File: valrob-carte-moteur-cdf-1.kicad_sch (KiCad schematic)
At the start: 48 parts, among them J1 USB_C_Receptacle_USB2.0_14P, J2 Conn_01x02, J3 Conn_01x02, J4 Conn_01x04_Pin, J5 Conn_01x08, J6 Conn_01x02, J7 Conn_01x02, J8 Conn_01x08, SW1 SW_Push, SW2 SW_Push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

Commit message: schem: add components footprints
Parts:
- C4, C7: footprint (none) -> Capacitor_SMD:C_0603_1608Metric
- C6: footprint (none) -> Capacitor_SMD:C_0805_2012Metric
- D4: footprint (none) -> Diode_SMD:D_SOD-123
- J2, J3, J6, J7: footprint (none) -> Connector_JST:JST_XH_S2B-XH-A_1x02_P2.50mm_Horizontal
- J5, J8: footprint (none) -> Connector_Molex:Molex_PicoBlade_53048-0810_1x08_P1.25mm_Horizontal
- R4: footprint (none) -> Resistor_SMD:R_0603_1608Metric
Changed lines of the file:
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@@
 			)
 		)
-		(property "Footprint" ""
+		(property "Footprint" "Connector_JST:JST_XH_S2B-XH-A_1x02_P2.50mm_Horizontal"
 			(at 87.63 180.34 0)
 			(effects
@@
 			)
 		)
-		(property "Footprint" ""
+		(property "Footprint" "Connector_Molex:Molex_PicoBlade_53048-0810_1x08_P1.25mm_Horizontal"
 			(at 50.8 95.25 0)
 			(effects
@@
 			)
 		)
-		(property "Footprint" ""
+		(property "Footprint" "Diode_SMD:D_SOD-123"
 			(at 109.22 148.59 0)
 			(effects
@@
 			)
 		)
-		(property "Footprint" ""
+		(property "Footprint" "Connector_JST:JST_XH_S2B-XH-A_1x02_P2.50mm_Horizontal"
 			(at 266.7 114.3 0)
 			(effects
@@
 			)
 		)
-		(property "Footprint" ""
+		(property "Footprint" "Connector_Molex:Molex_PicoBlade_53048-0810_1x08_P1.25mm_Horizontal"
 			(at 90.17 95.25 0)
 			(effects
@@
 			)
 		)
-		(property "Footprint" ""
+		(property "Footprint" "Capacitor_SMD:C_0603_1608Metric"
 			(at 180.0352 40.64 0)
 			(effects
@@
 			)
 		)
-		(property "Footprint" ""
+		(property "Footprint" "Resistor_SMD:R_0603_1608Metric"
 			(at 98.552 148.59 90)
 			(effects
@@
 			)
 		)
-		(property "Footprint" ""
+		(property "Footprint" "Connector_JST:JST_XH_S2B-XH-A_1x02_P2.50mm_Horizontal"
 			(at 266.7 83.82 0)
 			(effects
@@
 			)
 		)
-		(property "Footprint" ""
+		(property "Footprint" "Capacitor_SMD:C_0603_1608Metric"
 			(at 90.4748 152.4 0)
 			(effects
@@
 			)
 		)
-		(property "Footprint" ""
+		(property "Footprint" "Connector_JST:JST_XH_S2B-XH-A_1x02_P2.50mm_Horizontal"
 			(at 107.95 180.34 0)
 			(effects
@@
 			)
 		)
-		(property "Footprint" ""
+		(property "Footprint" "Capacitor_SMD:C_0805_2012Metric"
 			(at 170.4848 40.64 0)
 			(effects

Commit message: schem: add ordering info to BOM
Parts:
- C3: footprint Capacitor_SMD:C_0402_1005Metric -> Capacitor_SMD:C_0603_1608Metric; JLCPCB Part # C15525 -> C19702; Manufacturer Part Number CL05A106MQ5NUNC -> CL10A106KP8NNNC
- C4, C7: Basic (none) -> Y; JLCPCB Part # (none) -> C14663; Manufacturer (none) -> YAGEO; Manufacturer Part Number (none) -> CC0603KRX7R9BB104
- C5: footprint Capacitor_SMD:C_0402_1005Metric -> Capacitor_SMD:C_0603_1608Metric; JLCPCB Part # C52923 -> C15849; Manufacturer Part Number CL05A105KA5NQNC -> CL10A105KB8NNNC
- C6: Basic (none) -> Y; JLCPCB Part # (none) -> C45783; Manufacturer (none) -> Samsung Electro-Mechanics; Manufacturer Part Number (none) -> CL21A226MAQNNNE
- D4: Basic (none) -> E; JLCPCB Part # (none) -> C19077392; Manufacturer (none) -> hongjiacheng; Manufacturer Part Number (none) -> BZT52B3V3
- J2, J3, J5, J6, J7, J8, U3: now left out of the parts list
- R4: Basic (none) -> Y; JLCPCB Part # (none) -> C22978; Manufacturer (none) -> Uniroyal Elec; Manufacturer Part Number (none) -> 0603WAF3301T5E
- R8, R9: footprint Resistor_SMD:R_0402_1005Metric -> Resistor_SMD:R_0603_1608Metric; JLCPCB Part # C25092 -> C23345; Manufacturer Part Number 0402WGF220JTCE -> 0603WAF220JT5E
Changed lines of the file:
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@@
 			)
 		)
-		(property "Footprint" "Capacitor_SMD:C_0402_1005Metric"
+		(property "Footprint" "Capacitor_SMD:C_0603_1608Metric"
 			(at 61.2648 135.89 0)
 			(effects
@@
 			)
 		)
-		(property "Manufacturer Part Number" "CL05A106MQ5NUNC"
+		(property "Manufacturer Part Number" "CL10A106KP8NNNC"
 			(at 62.23 132.08 0)
 			(effects
@@
 			)
 		)
-		(property "JLCPCB Part #" "C15525"
+		(property "JLCPCB Part #" "C19702"
 			(at 62.23 132.08 0)
 			(effects
@@
 		(unit 1)
 		(exclude_from_sim no)
-		(in_bom yes)
+		(in_bom no)
 		(on_board yes)
 		(dnp no)
@@
 			)
 		)
-		(property "Footprint" "Resistor_SMD:R_0402_1005Metric"
+		(property "Footprint" "Resistor_SMD:R_0603_1608Metric"
 			(at 247.65 61.722 90)
 			(effects
@@
 			)
 		)
-		(property "JLCPCB Part #" "C25092"
+		(property "JLCPCB Part #" "C23345"
 			(at 247.65 63.5 90)
 			(effects
@@
 			)
 		)
-		(property "Manufacturer Part Number" "0402WGF220JTCE"
+		(property "Manufacturer Part Number" "0603WAF220JT5E"
 			(at 247.65 63.5 90)
 			(effects
@@
 		(unit 1)
 		(exclude_from_sim no)
-		(in_bom yes)
+		(in_bom no)
 		(on_board yes)
 		(dnp no)
@@
 			)
 		)
-		(property "Footprint" "Resistor_SMD:R_0402_1005Metric"
+		(property "Footprint" "Resistor_SMD:R_0603_1608Metric"
 			(at 247.65 62.738 90)
 			(effects
@@
 			)
 		)
-		(property "JLCPCB Part #" "C25092"
+		(property "JLCPCB Part #" "C23345"
 			(at 247.65 60.96 90)
 			(effects
@@
 			)
 		)
-		(property "Manufacturer Part Number" "0402WGF220JTCE"
+		(property "Manufacturer Part Number" "0603WAF220JT5E"
 			(at 247.65 60.96 90)
 			(effects
@@
 			)
 		)
+		(property "Basic" "E"
+			(at 109.22 148.59 90)
+			(effects
+				(font
+					(size 1.27 1.27)
+				)
+				(hide yes)
+			)
+		)
+		(property "JLCPCB Part #" "C19077392"
+			(at 109.22 148.59 90)
+			(effects
+				(font
+					(size 1.27 1.27)
+				)
+				(hide yes)
+			)
+		)
+		(property "Manufacturer" "hongjiacheng"
+			(at 109.22 148.59 90)
+			(effects
+				(font
+					(size 1.27 1.27)
+				)
+				(hide yes)
+			)
+		)
+		(property "Manufacturer Part Number" "BZT52B3V3"
+			(at 109.22 148.59 90)
+			(effects
+				(font
+					(size 1.27 1.27)
+				)
+				(hide yes)
+			)
+		)
 		(pin "1"
 		)
@@
 		(unit 1)
 		(exclude_from_sim no)
-		(in_bom yes)
+		(in_bom no)
 		(on_board yes)
 		(dnp no)
@@
 		(unit 1)
 		(exclude_from_sim no)
-		(in_bom yes)
+		(in_bom no)
 		(on_board yes)
 		(dnp no)
@@
 		(unit 1)
 		(exclude_from_sim no)
-		(in_bom yes)
+		(in_bom no)
 		(on_board yes)
 		(dnp no)
@@
 			)
 		)
+		(property "Basic" "Y"
+			(at 179.07 36.83 0)
+			(effects
+				(font
+					(size 1.27 1.27)
+				)
+				(hide yes)
+			)
+		)
+		(property "JLCPCB Part #" "C14663"
+			(at 179.07 36.83 0)
+			(effects
+				(font
+					(size 1.27 1.27)
+				)
+				(hide yes)
+			)
+		)
+		(property "Manufacturer" "YAGEO"
+			(at 179.07 36.83 0)
+			(effects
+				(font
+					(size 1.27 1.27)
+				)
+				(hide yes)
+			)
+		)
+		(property "Manufacturer Part Number" "CC0603KRX7R9BB104"
+			(at 179.07 36.83 0)
+			(effects
+				(font
+					(size 1.27 1.27)
+				)
+				(hide yes)
+			)
+		)
 		(pin "2"
 		)
@@
 			)
 		)
+		(property "Basic" "Y"
+			(at 100.33 148.59 0)
+			(effects
+				(font
+					(size 1.27 1.27)
+				)
+				(hide yes)
+			)
+		)
+		(property "JLCPCB Part #" "C22978"
+			(at 100.33 148.59 0)
+			(effects
+				(font
+					(size 1.27 1.27)
+				)
+				(hide yes)
+			)
+		)
+		(property "Manufacturer" "Uniroyal Elec"
+			(at 100.33 148.59 0)
+			(effects
+				(font
+					(size 1.27 1.27)
+				)
+				(hide yes)
+			)
+		)
+		(property "Manufacturer Part Number" "0603WAF3301T5E"
+			(at 100.33 148.59 0)
+			(effects
+				(font
+					(size 1.27 1.27)
+				)
+				(hide yes)
+			)
+		)
 		(pin "2"
 		)
@@
 		(unit 1)
 		(exclude_from_sim no)
-		(in_bom yes)
+		(in_bom no)
 		(on_board yes)
 		(dnp no)
@@
 			)
 		)
-		(property "Footprint" "Capacitor_SMD:C_0402_1005Metric"
+		(property "Footprint" "Capacitor_SMD:C_0603_1608Metric"
 			(at 129.8448 63.5 0)
 			(effects
@@
 			)
 		)
-		(property "Manufacturer Part Number" "CL05A105KA5NQNC"
+		(property "Manufacturer Part Number" "CL10A105KB8NNNC"
 			(at 130.81 59.69 0)
 			(effects
@@
 			)
 		)
-		(property "JLCPCB Part #" "C52923"
+		(property "JLCPCB Part #" "C15849"
 			(at 130.81 59.69 0)
 			(effects
@@
 			)
 		)
+		(property "Basic" "Y"
+			(at 91.44 148.59 0)
+			(effects
+				(font
+					(size 1.27 1.27)
+				)
+				(hide yes)
+			)
+		)
+		(property "JLCPCB Part #" "C14663"
+			(at 91.44 148.59 0)
+			(effects
+				(font
+					(size 1.27 1.27)
+				)
+				(hide yes)
+			)
+		)
+		(property "Manufacturer" "YAGEO"
+			(at 91.44 148.59 0)
+			(effects
+				(font
+					(size 1.27 1.27)
+				)
+				(hide yes)
+			)
+		)
+		(property "Manufacturer Part Number" "CC0603KRX7R9BB104"
+			(at 91.44 148.59 0)
+			(effects
+				(font
+					(size 1.27 1.27)
+				)
+				(hide yes)
+			)
+		)
 		(pin "2"
 		)
@@
 		(unit 1)
 		(exclude_from_sim no)
-		(in_bom yes)
+		(in_bom no)
 		(on_board yes)
 		(dnp no)
@@
 			(at 171.45 36.83 0)
 			(effects
+				(font
+					(size 1.27 1.27)
+				)
+				(hide yes)
+			)
+		)
+		(property "Basic" "Y"
+			(at 171.45 36.83 0)
+			(effects
+				(font
+					(size 1.27 1.27)
+				)
+				(hide yes)
+			)
+		)
+		(property "JLCPCB Part #" "C45783"
+			(at 171.45 36.83 0)
+			(effects
+				(font
+					(size 1.27 1.27)
+				)
+				(hide yes)
+			)
+		)
+		(property "Manufacturer" "Samsung Electro-Mechanics "
+			(at 171.45 36.83 0)
+			(effects
+				(font
+					(size 1.27 1.27)
+				)
+				(hide yes)
+			)
+		)
+		(property "Manufacturer Part Number" "CL21A226MAQNNNE"
+			(at 171.45 36.83 0)
+			(effects

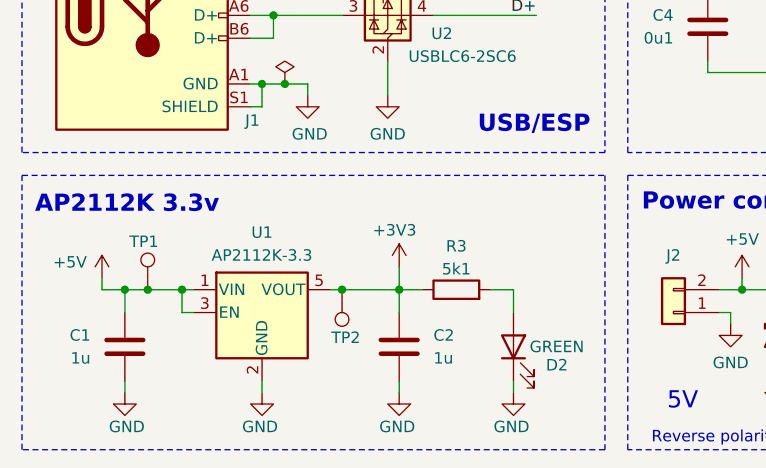
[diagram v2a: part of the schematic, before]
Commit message: schem: add ldo reverse current protection diode
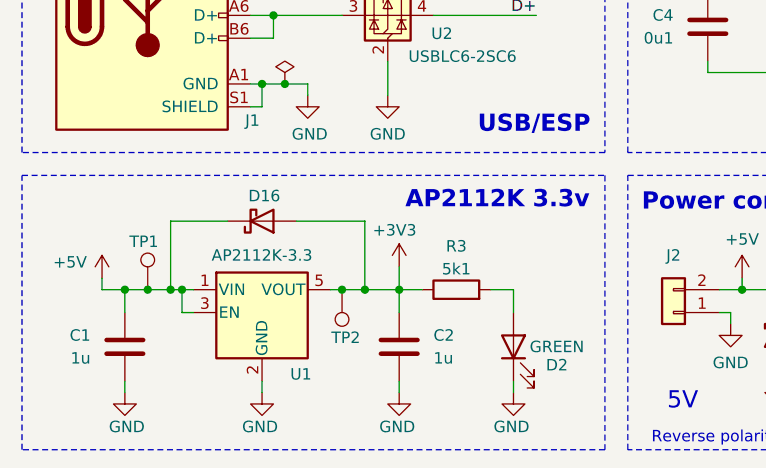
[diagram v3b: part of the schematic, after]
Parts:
- added D16: D_Schottky, Diode_SMD:D_SMA, symbol Device:D_Schottky
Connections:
- net +3V3: now also D16.2 (A)
- net +5V: now also D16.1 (K)
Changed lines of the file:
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@@
 	(text "AP2112K 3.3v"
 		(exclude_from_sim no)
-		(at 26.924 168.402 0)
+		(at 68.072 167.894 0)
 		(effects
 			(font
@@
 	)
 	(junction
+		(at 31.75 177.8)
+		(diameter 0)
+		(color 0 0 0 0)
+	)
+	(junction
 		(at 179.07 29.21)
 		(diameter 0)
@@
 	)
 	(junction
+		(at 53.34 177.8)
+		(diameter 0)
+		(color 0 0 0 0)
+	)
+	(junction
 		(at 109.22 143.51)
 		(diameter 0)
@@
 	(wire
 		(pts
+			(xy 53.34 177.8) (xy 57.15 177.8)
+		)
+		(stroke
+			(width 0)
+			(type default)
+		)
+	)
+	(wire
+		(pts
 			(xy 92.71 180.34) (xy 93.98 180.34)
 		)
@@
 	(wire
 		(pts
+			(xy 31.75 177.8) (xy 33.02 177.8)
+		)
+		(stroke
+			(width 0)
+			(type default)
+		)
+	)
+	(wire
+		(pts
 			(xy 234.95 111.76) (xy 242.57 111.76)
 		)
@@
 	(wire
 		(pts
+			(xy 53.34 170.18) (xy 53.34 177.8)
+		)
+		(stroke
+			(width 0)
+			(type default)
+		)
+	)
+	(wire
+		(pts
 			(xy 92.71 177.8) (xy 95.25 177.8)
 		)
@@
 	(wire
 		(pts
-			(xy 50.8 177.8) (xy 57.15 177.8)
+			(xy 50.8 177.8) (xy 53.34 177.8)
 		)
 		(stroke
@@
 	(wire
 		(pts
-			(xy 29.21 177.8) (xy 33.02 177.8)
+			(xy 29.21 177.8) (xy 31.75 177.8)
 		)
 		(stroke
@@
 	(wire
 		(pts
+			(xy 31.75 170.18) (xy 31.75 177.8)
+		)
+		(stroke
+			(width 0)
+			(type default)
+		)
+	)
+	(wire
+		(pts
 			(xy 25.4 92.71) (xy 45.72 92.71)
 		)
@@
 	(wire
 		(pts
+			(xy 45.72 170.18) (xy 53.34 170.18)
+		)
+		(stroke
+			(width 0)
+			(type default)
+		)
+	)
+	(wire
+		(pts
 			(xy 179.07 29.21) (xy 179.07 33.02)
 		)
@@
 	(wire
 		(pts
+			(xy 38.1 170.18) (xy 31.75 170.18)
+		)
+		(stroke
+			(width 0)
+			(type default)
+		)
+	)
+	(wire
+		(pts
 			(xy 33.02 180.34) (xy 34.29 180.34)
 		)
@@
 		(on_board yes)
 		(dnp no)
-		(fields_autoplaced yes)
 		(property "Reference" "U1"
-			(at 41.91 171.45 0)
+			(at 46.228 187.198 0)
 			(effects
 				(font
@@
 					(unit 1)
 				)
+			)
+		)
+	)
+	(symbol
+		(lib_id "Device:D_Schottky")
+		(at 41.91 170.18 0)
+		(mirror x)
+		(unit 1)
+		(exclude_from_sim no)
+		(in_bom yes)
+		(on_board yes)
+		(dnp no)
+		(property "Reference" "D16"
+			(at 42.164 167.386 0)
+			(effects
+				(font
+					(size 1.27 1.27)
+				)
+			)
+		)
+		(property "Value" "D_Schottky"
+			(at 41.5925 173.99 0)
+			(effects
+				(font
+					(size 1.27 1.27)
+				)
+				(hide yes)
+			)
+		)
+		(property "Footprint" "Diode_SMD:D_SMA"
+			(at 41.91 170.18 0)
+			(effects
+				(font
+					(size 1.27 1.27)
+				)
+				(hide yes)
+			)
+		)
+		(property "Datasheet" "~"
+			(at 41.91 170.18 0)
+			(effects
+				(font
+					(size 1.27 1.27)
+				)
+				(hide yes)
+			)
+		)
+		(property "Description" "Schottky diode"
+			(at 41.91 170.18 0)
+			(effects
+				(font
+					(size 1.27 1.27)
+				)
+				(hide yes)
+			)
+		)
+		(property "Manufacturer" "Microdiode Semiconductor (MDD)"
+			(at 41.91 170.18 0)
+			(effects
+				(font
+					(size 1.27 1.27)
+				)
+				(hide yes)
+			)
+		)
+		(property "Manufacturer Part Number" "SS54"
+			(at 41.91 170.18 0)
+			(effects
+				(font
+					(size 1.27 1.27)
+				)
+				(hide yes)
+			)
+		)
+		(property "Basic" "Y"
+			(at 41.91 170.18 0)
+			(effects
+				(font
+					(size 1.27 1.27)
+				)
+				(hide yes)
+			)
+		)
+		(property "JLCPCB Part #" "C22452"
+			(at 41.91 170.18 0)
+			(effects
+				(font
+					(size 1.27 1.27)
+				)
+				(hide yes)
+			)
+		)
+		(pin "2"
+		)
+		(pin "1"
+		)
+		(instances
+			(project "valrob-carte-moteur-cdf-1"
+				(path "/b89f538c-def5-4450-bb35-40e96c574400"
+					(reference "D16")
+					(unit 1)
+				)

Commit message: pcb: add DRV8874 dc motor driver routing
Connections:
- net Vsense: now also U3.17 (GPIO9/TOUCH9/ADC1_CH8/FSPIHD/SUBSPIHD); no longer U3.39 (GPIO1/TOUCH1/ADC1_CH0)
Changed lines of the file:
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@@
+	)
+	(no_connect
+		(at 234.95 71.12)
 	)
 	(no_connect
@@
 	)
 	(no_connect
-		(at 234.95 91.44)
-	)
-	(no_connect
 		(at 143.51 60.96)
 	)
@@
 	(wire
 		(pts
+			(xy 234.95 91.44) (xy 242.57 91.44)
+		)
+		(stroke
+			(width 0)
+			(type default)
+		)
+	)
+	(wire
+		(pts
 			(xy 33.02 177.8) (xy 34.29 177.8)
 		)
@@
 		(pts
 			(xy 179.07 29.21) (xy 189.23 29.21)
-		)
-		(stroke
-			(width 0)
-			(type default)
-		)
-	)
-	(wire
-		(pts
-			(xy 234.95 71.12) (xy 242.57 71.12)
 		)
 		(stroke
@@
 		)
 	)
-	(label "Vsense"
-		(at 242.57 71.12 180)
-		(effects
-			(font
-				(size 1.27 1.27)
-			)
-			(justify right bottom)
-		)
-	)
 	(label "D-"
 		(at 72.39 144.78 180)
@@
 		(effects
 			(font
+				(size 1.27 1.27)
+			)
+			(justify right bottom)
+		)
+	)
+	(label "Vsense"
+		(at 242.57 91.44 180)
+		(effects
+			(font

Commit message: add spare gpios
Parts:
- added J9: Conn_01x04_Pin, Connector_PinHeader_2.54mm:PinHeader_1x04_P2.54mm_Vertical, symbol Connector:Conn_01x04_Pin
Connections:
- net CHIP_PU: now also C5.2; no longer C5.1
- net GND: now also C5.1; no longer C5.2
- net at U3.32 (MTCK/GPIO39/CLK_OUT3/SUBSPICS1): now also J9.1 (Pin_1)
- net at U3.33 (MTDO/GPIO40/CLK_OUT2): now also J9.2 (Pin_2)
- net at U3.34 (MTDI/GPIO41/CLK_OUT1): now also J9.3 (Pin_3)
- net at U3.35 (MTMS/GPIO42): now also J9.4 (Pin_4)
- no-connect marks 15 -> 11
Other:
- moved on the sheet: C5, R5
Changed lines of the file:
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@@
 	(text "EN RC delay"
 		(exclude_from_sim no)
-		(at 122.174 53.594 0)
+		(at 116.078 46.736 0)
 		(effects
 			(font
@@
 	)
 	(no_connect
-		(at 143.51 73.66)
-	)
-	(no_connect
 		(at 234.95 78.74)
 	)
@@
 		(at 45.72 85.09)
 	)
-	(no_connect
-		(at 143.51 68.58)
-	)
-	(no_connect
-		(at 143.51 76.2)
-	)
-	(no_connect
-		(at 143.51 71.12)
-	)
 	(wire
 		(pts
@@
 	(wire
 		(pts
-			(xy 130.81 53.34) (xy 130.81 55.88)
-		)
-		(stroke
-			(width 0)
-			(type default)
-		)
-	)
-	(wire
-		(pts
 			(xy 114.3 181.61) (xy 114.3 180.34)
 		)
@@
 	(wire
 		(pts
+			(xy 143.51 73.66) (xy 135.89 73.66)
+		)
+		(stroke
+			(width 0)
+			(type default)
+		)
+	)
+	(wire
+		(pts
 			(xy 60.96 110.49) (xy 64.77 110.49)
 		)
@@
 	(wire
 		(pts
+			(xy 120.65 54.61) (xy 120.65 53.34)
+		)
+		(stroke
+			(width 0)
+			(type default)
+		)
+	)
+	(wire
+		(pts
 			(xy 238.76 116.84) (xy 238.76 109.22)
 		)
@@
 	(wire
 		(pts
+			(xy 143.51 71.12) (xy 135.89 71.12)
+		)
+		(stroke
+			(width 0)
+			(type default)
+		)
+	)
+	(wire
+		(pts
 			(xy 40.64 111.76) (xy 40.64 110.49)
 		)
@@
 	(wire
 		(pts
+			(xy 120.65 53.34) (xy 121.92 53.34)
+		)
+		(stroke
+			(width 0)
+			(type default)
+		)
+	)
+	(wire
+		(pts
 			(xy 130.81 53.34) (xy 143.51 53.34)
 		)
@@
 	(wire
 		(pts
-			(xy 130.81 63.5) (xy 130.81 64.77)
-		)
-		(stroke
-			(width 0)
-			(type default)
-		)
-	)
-	(wire
-		(pts
 			(xy 132.08 185.42) (xy 134.62 185.42)
 		)
@@
 	(wire
 		(pts
+			(xy 143.51 68.58) (xy 135.89 68.58)
+		)
+		(stroke
+			(width 0)
+			(type default)
+		)
+	)
+	(wire
+		(pts
 			(xy 44.45 128.27) (xy 44.45 129.54)
 		)
@@
 	(wire
 		(pts
+			(xy 129.54 53.34) (xy 130.81 53.34)
+		)
+		(stroke
+			(width 0)
+			(type default)
+		)
+	)
+	(wire
+		(pts
 			(xy 234.95 81.28) (xy 242.57 81.28)
 		)
@@
 	(wire
 		(pts
+			(xy 143.51 76.2) (xy 135.89 76.2)
+		)
+		(stroke
+			(width 0)
+			(type default)
+		)
+	)
+	(wire
+		(pts
 			(xy 45.72 170.18) (xy 53.34 170.18)
 		)
@@
 	(symbol
 		(lib_id "Device:C")
-		(at 130.81 59.69 0)
-		(mirror y)
+		(at 125.73 53.34 90)
+		(mirror x)
 		(unit 1)
 		(exclude_from_sim no)
@@
 		(dnp no)
 		(property "Reference" "C5"
-			(at 127 58.4199 0)
+			(at 125.73 47.244 90)
 			(effects
 				(font
 					(size 1.27 1.27)
 				)
-				(justify left)
 			)
 		)
 		(property "Value" "1u"
-			(at 127 60.9599 0)
+			(at 125.73 49.784 90)
 			(effects
 				(font
 					(size 1.27 1.27)
 				)
-				(justify left)
 			)
 		)
 		(property "Footprint" "Capacitor_SMD:C_0603_1608Metric"
-			(at 129.8448 63.5 0)
+			(at 129.54 54.3052 0)
 			(effects
 				(font
@@
 		)
 		(property "Datasheet" "~"
-			(at 130.81 59.69 0)
+			(at 125.73 53.34 0)
 			(effects
 				(font
@@
 		)
 		(property "Description" "Unpolarized capacitor"
-			(at 130.81 59.69 0)
+			(at 125.73 53.34 0)
 			(effects
 				(font
@@
 		)
 		(property "Manufacturer" "Samsung Electro-Mechanics "
-			(at 130.81 59.69 0)
+			(at 125.73 53.34 0)
 			(effects
 				(font
@@
 		)
 		(property "Manufacturer Part Number" "CL10A105KB8NNNC"
-			(at 130.81 59.69 0)
+			(at 125.73 53.34 0)
 			(effects
 				(font
@@
 		)
 		(property "Basic" "Y"
-			(at 130.81 59.69 0)
+			(at 125.73 53.34 0)
 			(effects
 				(font
@@
 		)
 		(property "JLCPCB Part #" "C15849"
-			(at 130.81 59.69 0)
+			(at 125.73 53.34 0)
 			(effects
 				(font
@@
 	(symbol
 		(lib_id "Device:R")
-		(at 130.81 48.26 0)
-		(mirror x)
+		(at 130.81 48.26 180)
 		(unit 1)
 		(exclude_from_sim no)
@@
 		(dnp no)
 		(property "Reference" "R5"
-			(at 128.27 46.9899 0)
+			(at 133.35 46.9899 0)
 			(effects
 				(font
@@
 		)
 		(property "Value" "10k"
-			(at 128.27 49.5299 0)
+			(at 133.35 49.5299 0)
 			(effects
 				(font
@@
 		)
 		(property "Footprint" "Resistor_SMD:R_0603_1608Metric"
-			(at 129.032 48.26 90)
+			(at 132.588 48.26 90)
 			(effects
 				(font
@@
 	(symbol
 		(lib_id "power:GND")
-		(at 130.81 64.77 0)
+		(at 120.65 54.61 0)
 		(unit 1)
 		(exclude_from_sim no)
@@
 		(dnp no)
 		(property "Reference" "#PWR018"
-			(at 130.81 71.12 0)
+			(at 120.65 60.96 0)
 			(effects
 				(font
@@
 		)
 		(property "Value" "GND"
-			(at 130.81 69.088 0)
+			(at 120.65 58.928 0)
 			(effects
 				(font
@@
 		)
 		(property "Footprint" ""
-			(at 130.81 64.77 0)
+			(at 120.65 54.61 0)
 			(effects
 				(font
@@
 		)
 		(property "Datasheet" ""
-			(at 130.81 64.77 0)
+			(at 120.65 54.61 0)
 			(effects
 				(font
@@
 		)
 		(property "Description" "Power symbol creates a global label with name \"GND\" , ground"
-			(at 130.81 64.77 0)
+			(at 120.65 54.61 0)
 			(effects
 				(font
@@
 					(unit 1)
 				)
+			)
+		)
+	)
+	(symbol
+		(lib_id "Connector:Conn_01x04_Pin")
+		(at 130.81 71.12 0)
+		(unit 1)
+		(exclude_from_sim no)
+		(in_bom no)
+		(on_board yes)
+		(dnp no)
+		(property "Reference" "J9"
+			(at 131.064 65.786 90)
+			(effects
+				(font
+					(size 1.27 1.27)
+				)
+			)
+		)
+		(property "Value" "Conn_01x04_Pin"
+			(at 128.27 72.39 90)
+			(effects
+				(font
+					(size 1.27 1.27)
+				)
+				(hide yes)
+			)
+		)
+		(property "Footprint" "Connector_PinHeader_2.54mm:PinHeader_1x04_P2.54mm_Vertical"
+			(at 130.81 71.12 0)
+			(effects
+				(font
+					(size 1.27 1.27)
+				)
+				(hide yes)
+			)
+		)
+		(property "Datasheet" "~"
+			(at 130.81 71.12 0)
+			(effects
+				(font
+					(size 1.27 1.27)
+				)
+				(hide yes)
+			)
+		)
+		(property "Description" "Generic connector, single row, 01x04, script generated"
+			(at 130.81 71.12 0)
+			(effects
+				(font
+					(size 1.27 1.27)
+				)
+				(hide yes)
+			)
+		)
+		(pin "4"
+		)
+		(pin "3"
+		)
+		(pin "2"
+		)
+		(pin "1"
+		)
+		(instances
+			(project "valrob-carte-moteur-cdf-1"
+				(path "/b89f538c-def5-4450-bb35-40e96c574400"
+					(reference "J9")
+					(unit 1)
+				)
